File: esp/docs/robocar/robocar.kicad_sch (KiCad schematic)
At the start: 0 parts

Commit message: [ADD] Kicad esp32 s3 C1 component to robocar library
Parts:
- added U1: ~, symbol robocar:P1_Standard_Dev_Kit
- added U2: ~, symbol robocar:mini_v6.7_pro_flipsky
- added U3: ~, symbol robocar:D500_Lidar_Kit
- added U4: ESP32-S3-DEVKITC-1-N16R8V, ESP32-S3-DEVKITC-1-N16R8V:XCVR_ESP32-S3-DEVKITC-1-N16R8V, symbol ESP32-S3-DEVKITC-1-N16R8V:ESP32-S3-DEVKITC-1-N16R8V
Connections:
- new net 3V3: U4.J1_1 (3V3), U4.J1_2 (3V3)
- new net GND: U4.J1_22 (GND), U4.J3_1 (GND), U4.J3_21 (GND), U4.J3_22 (GND)

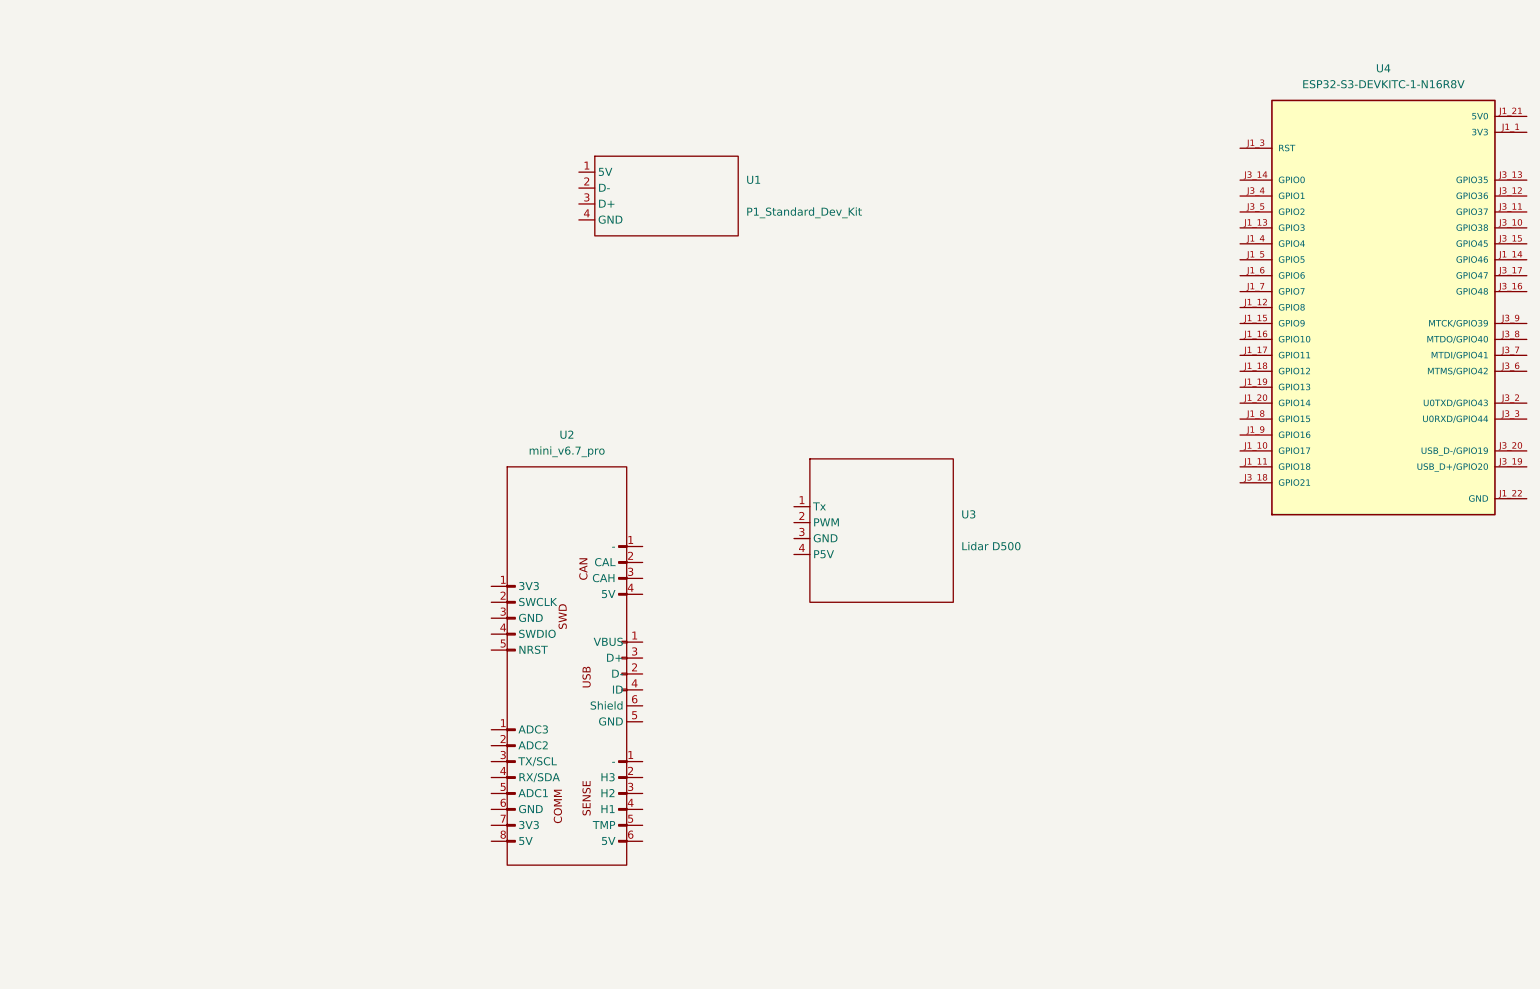
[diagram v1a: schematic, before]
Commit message: [ADD] Hardware architecture
- Updates to the esp component
- Updates to the gps component
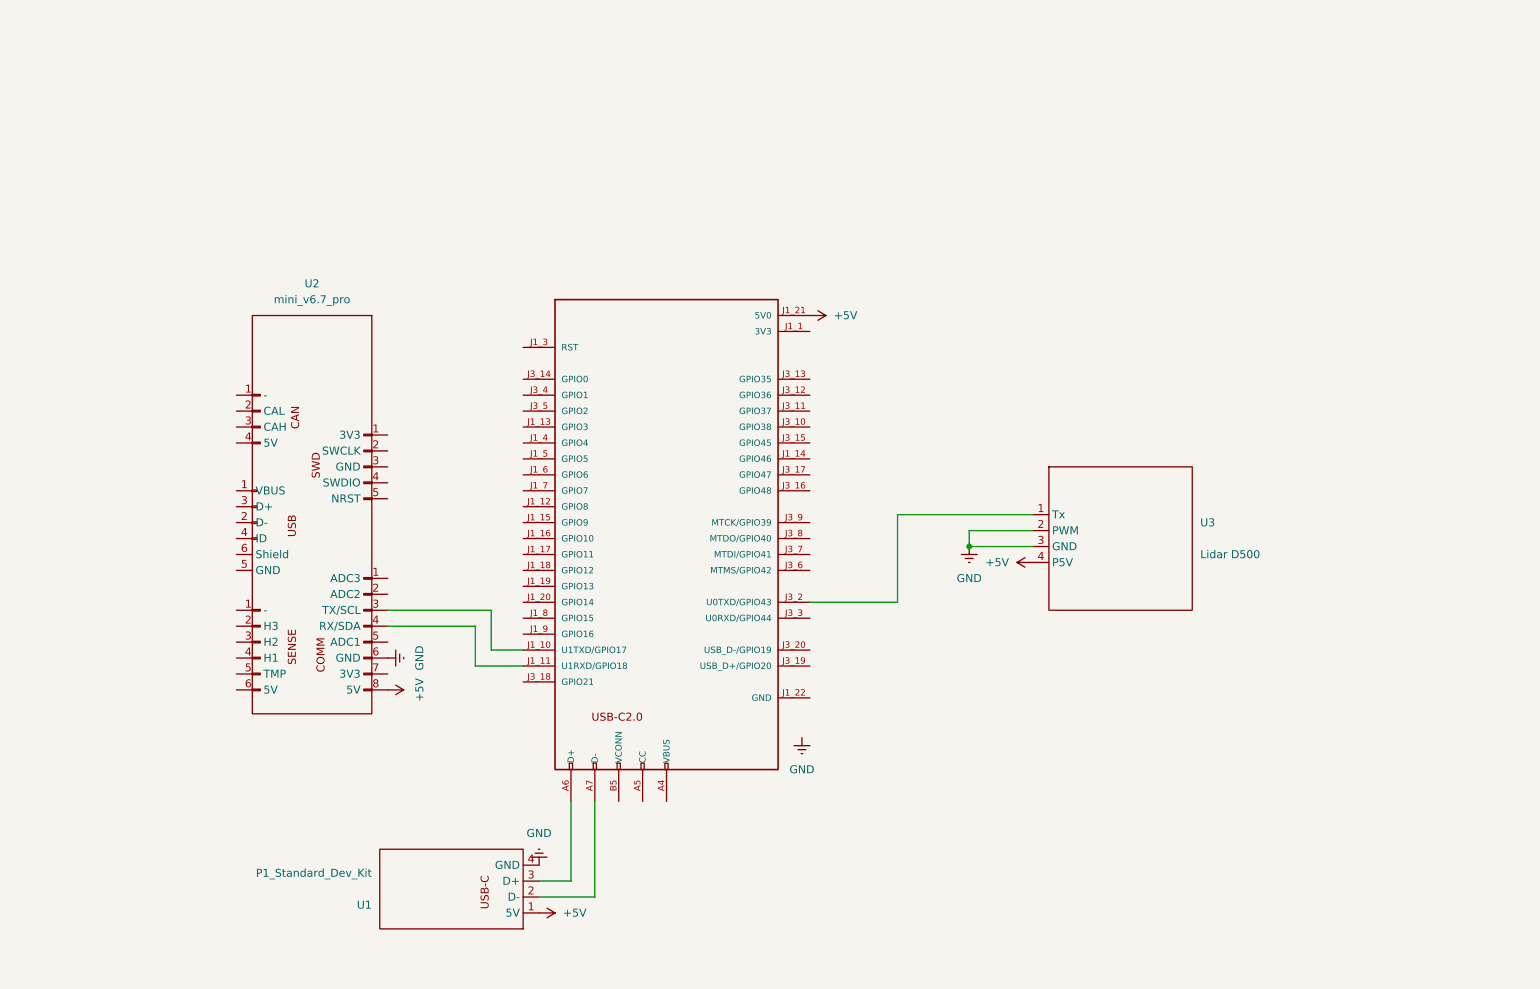
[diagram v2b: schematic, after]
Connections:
- net GND: now also U1.4 (GND), U2.6 (5V), U3.2 (PWM), U3.3 (GND)
- net at U2.3 (H2): now also U4.J1_10 (U1TXD/GPIO17)
- net at U2.4 (H1): now also U4.J1_11 (U1RXD/GPIO18)
- net +5V: now reaches U2.8 (5V)
- net +5V: now also U1.1 (5V), U3.4 (P5V), U4.J1_21 (5V0)
- net at U1.2 (D-): now also U4.A7 (D-)
- net at U1.3 (D+): now also U4.A6 (D+)
- net at U3.1 (Tx): now also U4.J3_2 (U0TXD/GPIO43)
- new net: U4.A9 (VBUS), U4.B4 (VBUS), U4.B9 (VBUS)
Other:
- moved on the sheet: U2, U3

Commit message: [UPD] Hardware schematic
- added no-connect symbols
- fixed mismatched tx rx conn on lidar
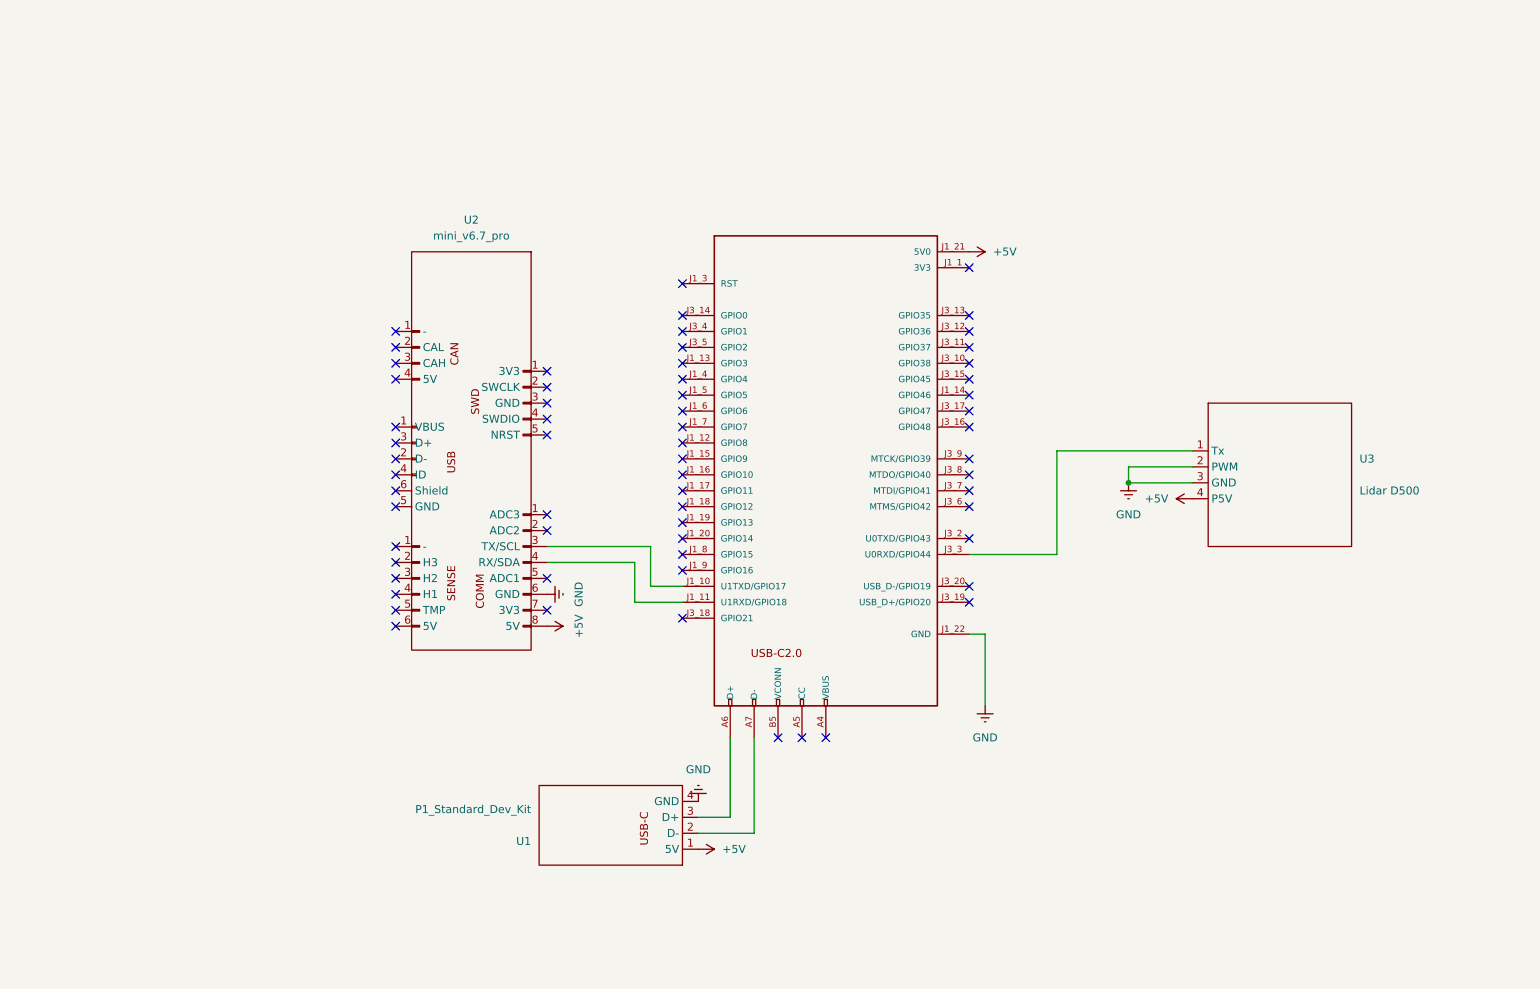
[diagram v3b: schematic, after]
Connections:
- net at U2.3 (H2): now also U4.J1_10 (U1TXD/GPIO17)
- net at U2.4 (H1): now also U4.J1_11 (U1RXD/GPIO18)
- net at U3.1 (Tx): now also U4.J3_3 (U0RXD/GPIO44); no longer U4.J3_2 (U0TXD/GPIO43)
- no-connect marks 0 -> 63
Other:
- title: (none) -> esp_connection
- moved on the sheet: U1, U2, U3

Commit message: [UPD] Added OAK-D Lite camera connection to esp32
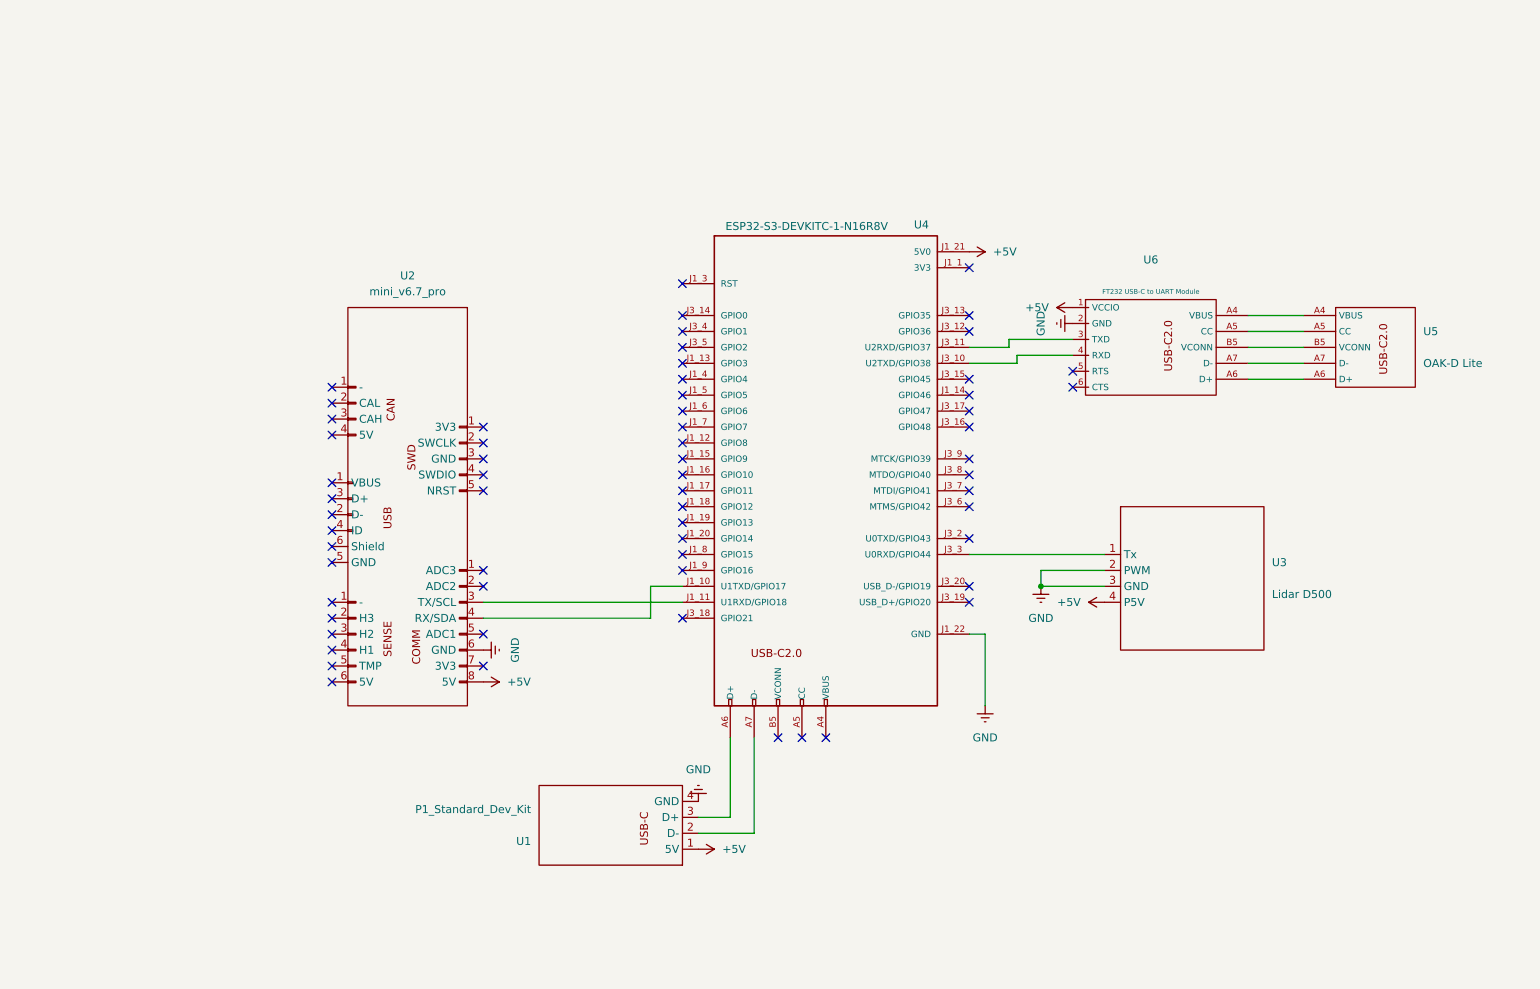
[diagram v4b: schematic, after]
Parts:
- added U5: ~, symbol robocar:OAK-D-Lite
- added U6: ~, symbol robocar:FT232_USB-C_to_UART_Module
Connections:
- net +5V: now also U6.1 (VCCIO)
- net GND: now also U6.2 (GND)
- net at U2.3 (H2): now also U4.J1_11 (U1RXD/GPIO18)
- net at U4.J1_10 (U1TXD/GPIO17): now also U2.4 (H1); no longer U2.3 (H2)
- net at U4.J3_10 (U2TXD/GPIO38): now also U6.4 (RXD)
- net at U4.J3_11 (U2RXD/GPIO37): now also U6.3 (TXD)
- new net: U5.A4 (VBUS), U6.A4 (VBUS)
- new net: U5.A5 (CC), U6.A5 (CC)
- new net: U5.A6 (D+), U6.A6 (D+)
- new net: U5.A7 (D-), U6.A7 (D-)
- new net: U6.A9 (VBUS), U6.B4 (VBUS), U6.B9 (VBUS)
- new net: U5.B5 (VCONN), U6.B5 (VCONN)
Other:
- moved on the sheet: U2, U3

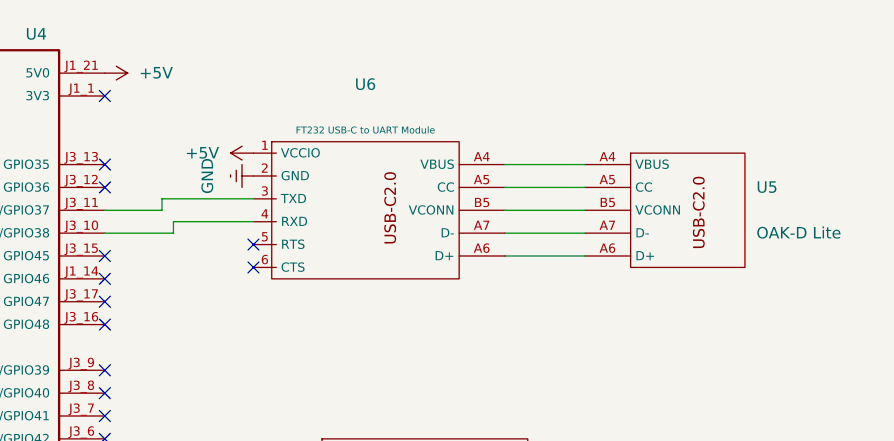
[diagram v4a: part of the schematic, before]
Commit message: [UPD] Switched OAK-D Lite to Recamera
- modification following-up the camera switch
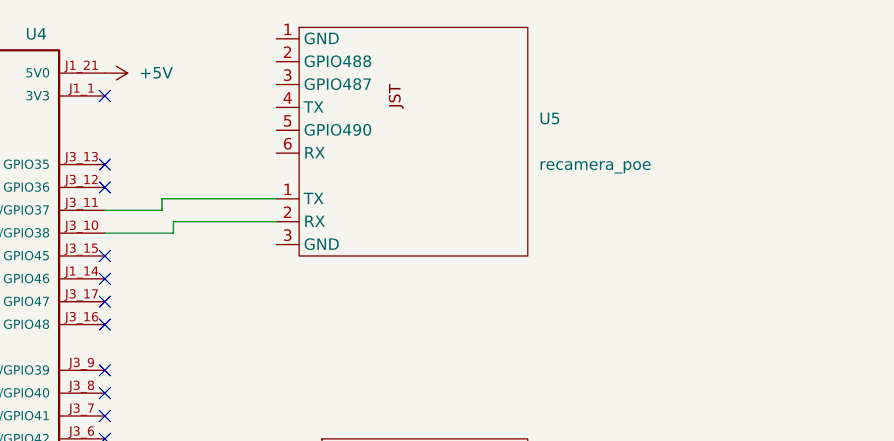
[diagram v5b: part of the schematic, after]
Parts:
- removed U5: ~, symbol robocar:OAK-D-Lite
- removed U6: ~, symbol robocar:FT232_USB-C_to_UART_Module
- added U5: ~, symbol robocar:recamera_poe
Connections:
- net at U2.3 (H2): now also U4.J1_11 (U1RXD/GPIO18)
- net at U2.4 (H1): now also U4.J1_10 (U1TXD/GPIO17)
- net at U4.J3_11 (U2RXD/GPIO37): now also U5.1 (TX)
- net at U4.J3_10 (U2TXD/GPIO38): now also U5.2 (RX)
- no-connect marks 63 -> 61

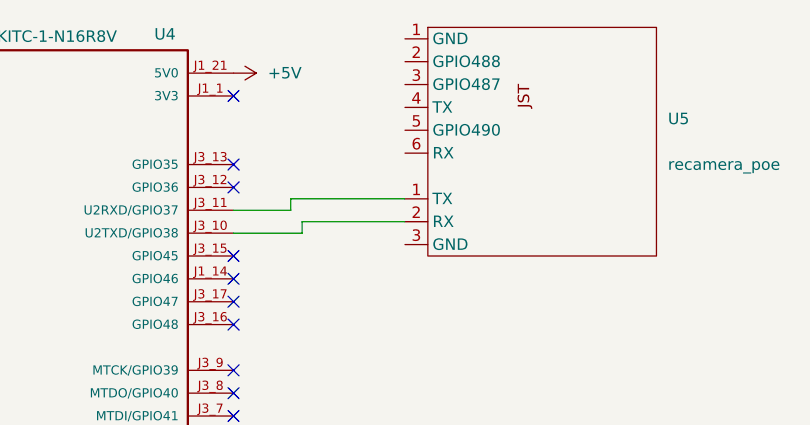
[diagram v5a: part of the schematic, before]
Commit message: [UPD] Added no connect symbols to hardware architecture
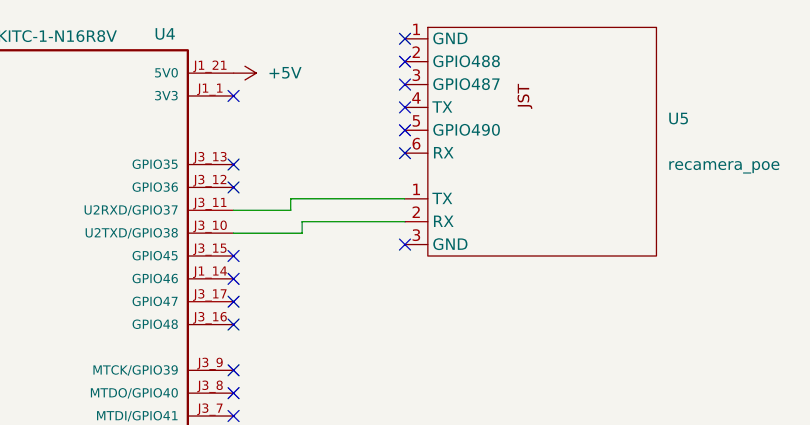
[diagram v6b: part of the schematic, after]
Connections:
- net at U2.3 (H2): now also U4.J1_11 (U1RXD/GPIO18)
- net at U2.4 (H1): now also U4.J1_10 (U1TXD/GPIO17)
- net at U5.1 (TX): now also U4.J3_11 (U2RXD/GPIO37)
- net at U5.2 (RX): now also U4.J3_10 (U2TXD/GPIO38)
- no-connect marks 61 -> 68
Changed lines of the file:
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@@
+	)
+	(no_connect
+		(at 191.77 55.88)
 	)
 	(no_connect
@@
 	(no_connect
 		(at 127 110.49)
+	)
+	(no_connect
+		(at 191.77 66.04)
 	)
 	(no_connect
@@
 	)
 	(no_connect
+		(at 191.77 78.74)
+	)
+	(no_connect
 		(at 149.86 137.16)
 	)
@@
 	(no_connect
 		(at 71.12 83.82)
+	)
+	(no_connect
+		(at 191.77 68.58)
+	)
+	(no_connect
+		(at 191.77 58.42)
 	)
 	(no_connect
@@
 	)
 	(no_connect
+		(at 191.77 60.96)
+	)
+	(no_connect
 		(at 127 107.95)
 	)
@@
 	)
 	(no_connect
+		(at 191.77 63.5)
+	)
+	(no_connect
